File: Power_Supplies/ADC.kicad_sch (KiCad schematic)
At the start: 22 parts, among them IC3 PCM1865DBT, U17 LM27761

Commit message: big things are coming...
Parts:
- removed C57, C61: 1uF, Capacitor_SMD:C_0805_2012Metric, symbol Device:C
- removed C58: 10uF, Capacitor_SMD:C_0805_2012Metric, symbol Device:C
- removed C59: 2.2uF, Capacitor_SMD:C_0805_2012Metric, symbol Device:C
- removed C60: 4.7uF, Capacitor_SMD:C_0805_2012Metric, symbol Device:C
- removed R74: 249k, Resistor_SMD:R_0603_1608Metric, symbol Device:R
- removed R75: 499k, Resistor_SMD:R_0603_1608Metric, symbol Device:R
- removed U17: LM27761, Package_SON:WSON-8-1EP_2x2mm_P0.5mm_EP0.9x1.6mm, symbol Regulator_SwitchedCapacitor:LM27761
- added C18: 10uF, Capacitor_SMD:C_0805_2012Metric, symbol Device:C
- added C23, C24: 1uF, Capacitor_SMD:C_0805_2012Metric, symbol Device:C
- added C25: 4.7uF, Capacitor_SMD:C_0805_2012Metric, symbol Device:C
- added C26: 2.2uF, Capacitor_SMD:C_0805_2012Metric, symbol Device:C
- added R15: 249k, Resistor_SMD:R_0603_1608Metric, symbol Device:R
- added R16: 499k, Resistor_SMD:R_0603_1608Metric, symbol Device:R
- added U8: LM27761, Package_SON:WSON-8-1EP_2x2mm_P0.5mm_EP0.9x1.6mm, symbol Regulator_SwitchedCapacitor:LM27761
- renumbered C32 to C11, C102 to C12, C107 to C13, C110 to C14, C111 to C15, C112 to C16, C113 to C17, C114 to C19, C115 to C20, C116 to C21, C117 to C22, C118 to C27, C119 to C28, IC3 to IC1
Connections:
- net -5V: now also C26.2, R15.1, U8.4 (VOUT)
- net 5V: now also C18.2, C23.2, U8.1 (VIN), U8.6 (EN)
- net DGND: now also C18.1, C23.1, C25.1, C26.1, R16.2, U8.2 (GND), U8.9 (PAD)
- new net: C24.1, U8.7 (C-)
- new net: C24.2, U8.8 (C+)
- new net: R15.2, R16.1, U8.5 (VFB)
- new net: C25.2, U8.3 (CPOUT)

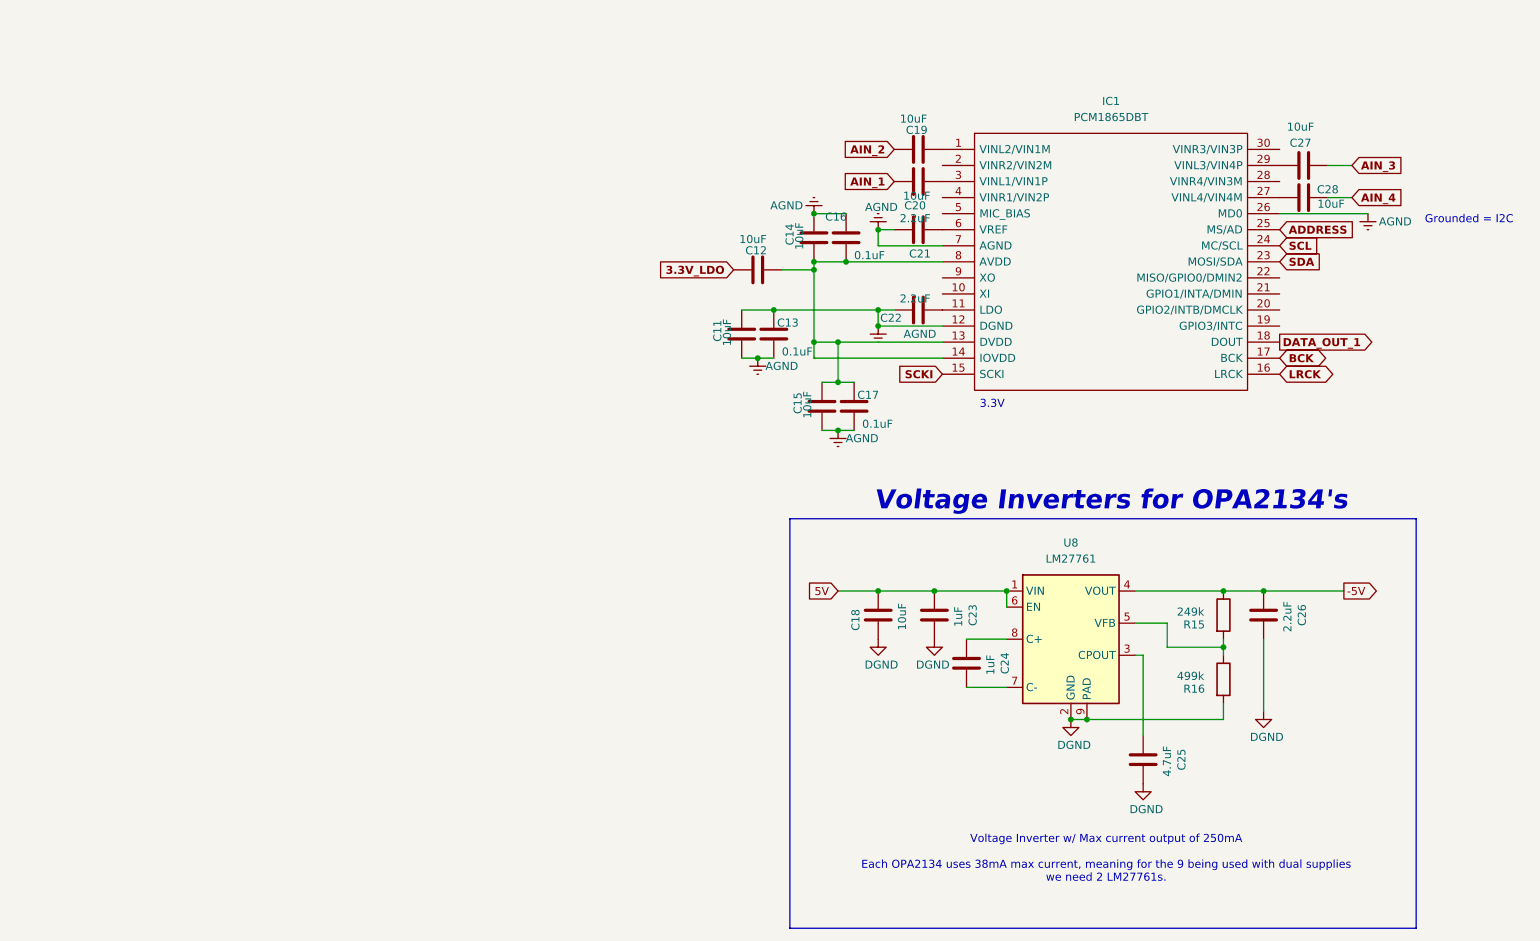
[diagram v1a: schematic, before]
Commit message: More XCORE PCB updates
Finished XTAG header, reinstated clock, worked on power pins
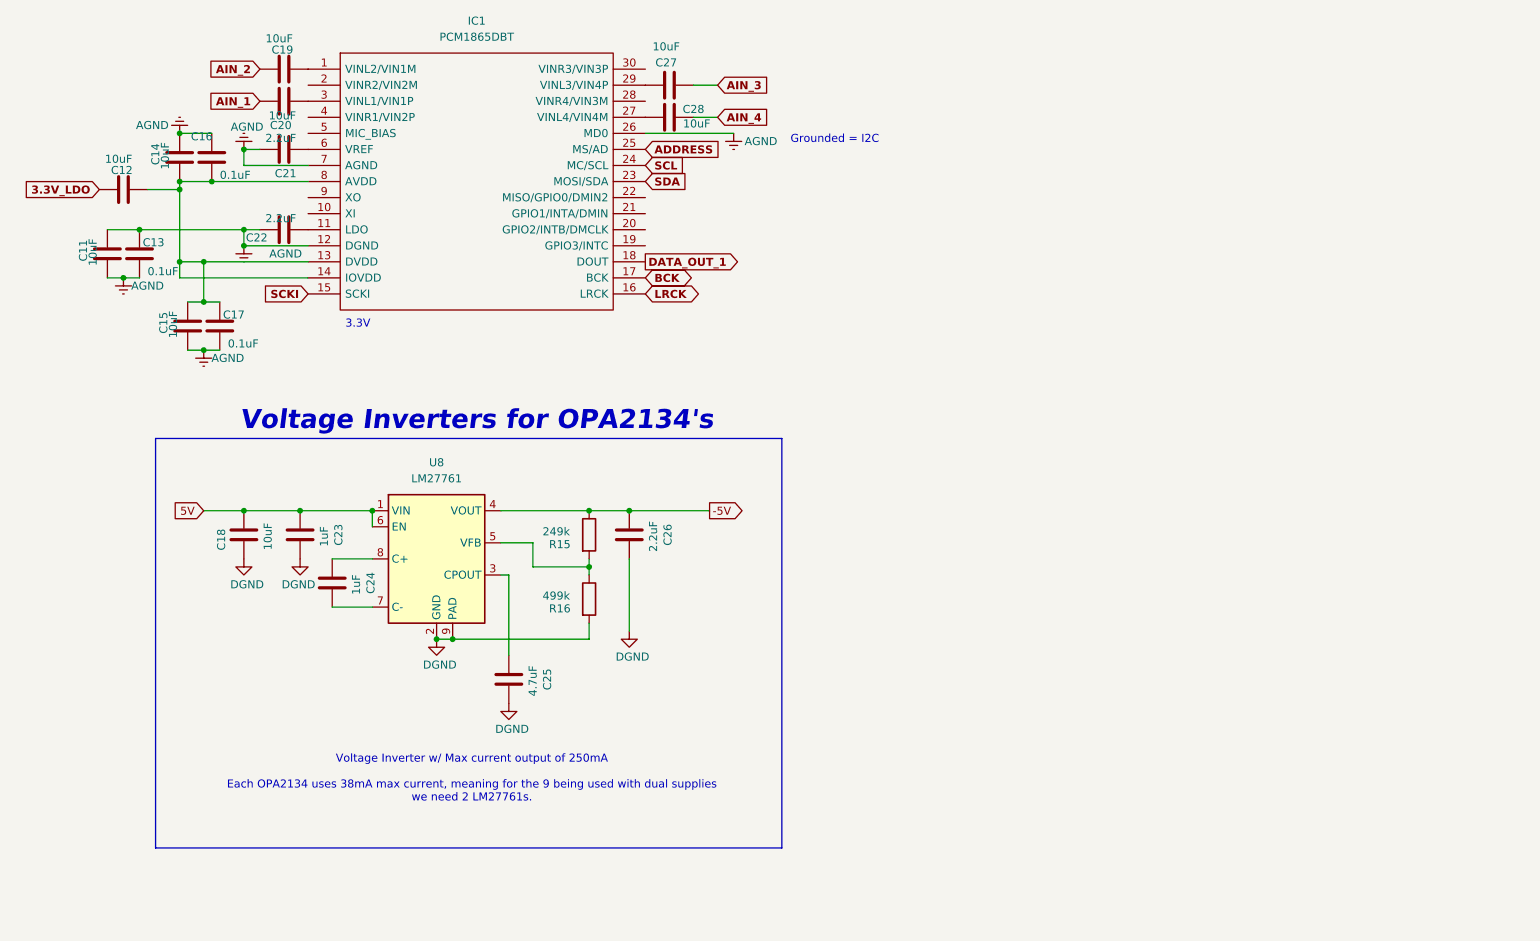
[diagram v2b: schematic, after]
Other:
- moved on the sheet: C11, C12, C13, C14, C15, C16, C17, C18, C19, C20, C21, C22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

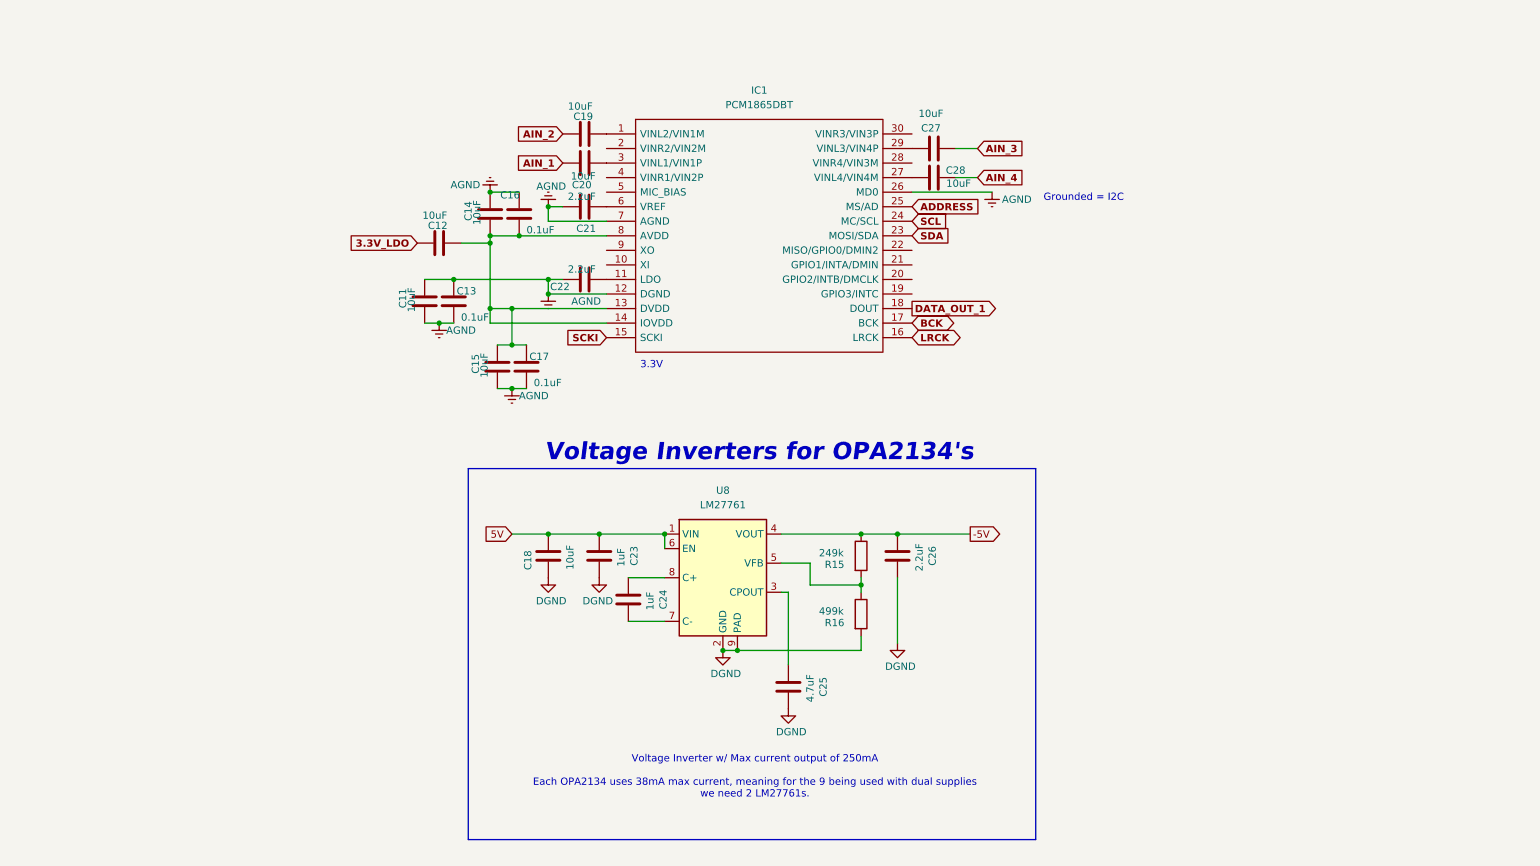
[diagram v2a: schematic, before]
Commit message: added both ADCs, added differential output to DACs
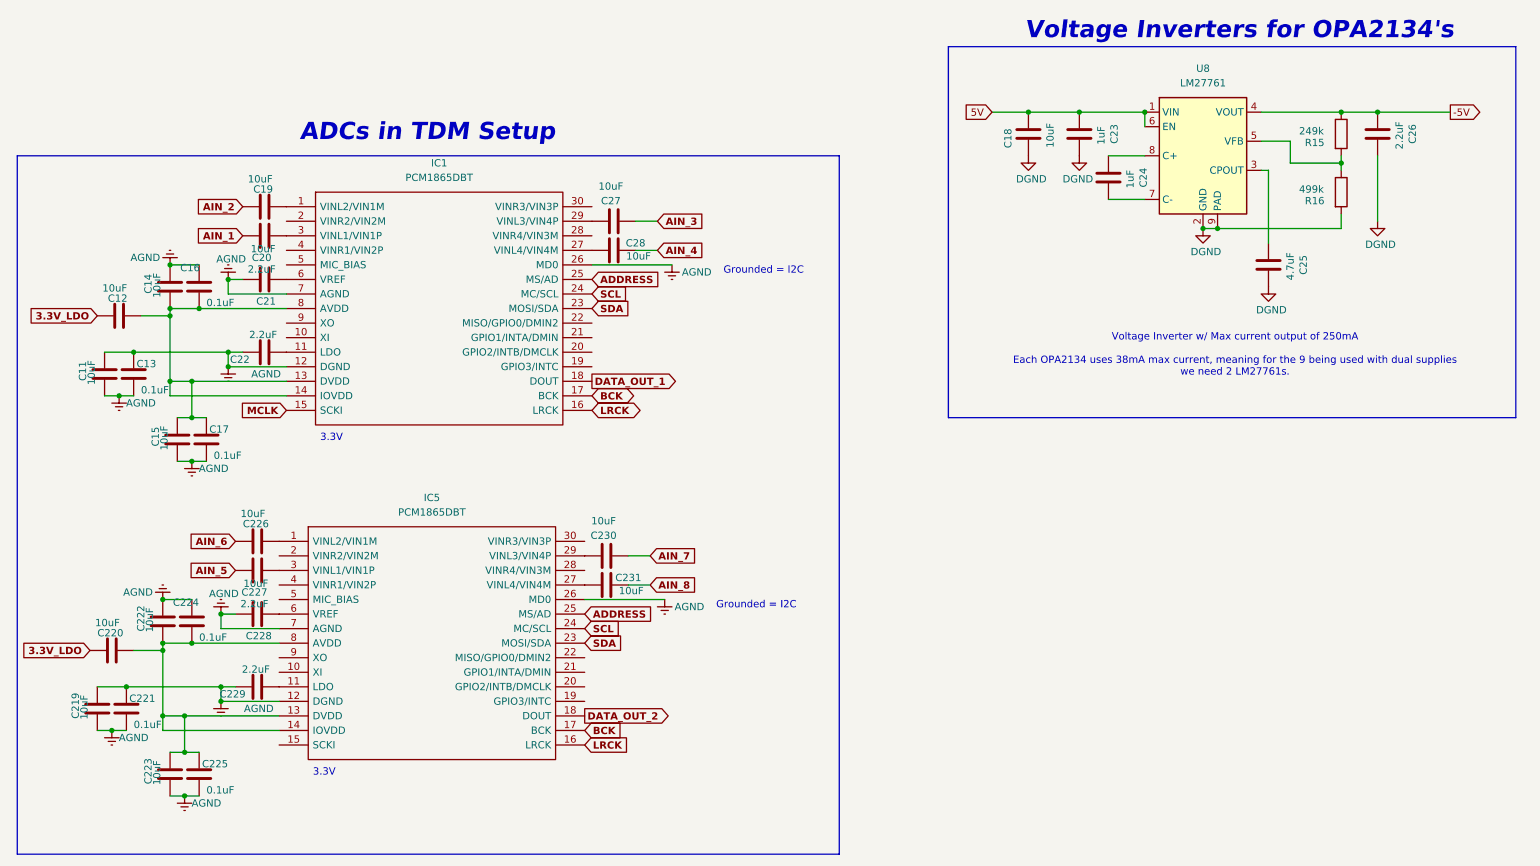
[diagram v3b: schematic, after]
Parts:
- added C219, C220, C222, C223, C226, C227, C230, C231: 10uF, Capacitor_SMD:C_0805_2012Metric, symbol Device:C
- added C221, C224, C225: 0.1uF, Capacitor_SMD:C_0805_2012Metric, symbol Device:C
- added C228, C229: 2.2uF, Capacitor_SMD:C_0805_2012Metric, symbol Device:C
- added IC5: PCM1865DBT, SamacSys_Parts:SOP50P640X120-30N, symbol SamacSys_Parts:PCM1865DBT
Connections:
- net 3.3V_LDO: now also C220.1
- net ADDRESS: now also IC5.25 (MS/AD)
- net AGND: now also C219.1, C219.2, C221.1, C221.2, C222.1, C223.2, C224.1, C225.2, C228.1, C229.1, IC5.12 (DGND), IC5.26 (MD0), IC5.7 (AGND)
- net BCK: now also IC5.17 (BCK)
- net LRCK: now also IC5.16 (LRCK)
- net SCL: now also IC5.24 (MC/SCL)
- net SDA: now also IC5.23 (MOSI/SDA)
- net SCKI renamed MCLK
- new net: C220.2, C222.2, C223.1, C224.2, C225.1, IC5.13 (DVDD), IC5.14 (IOVDD), IC5.8 (AVDD)
- new net: C229.2, IC5.11 (LDO)
- new net: C231.1, IC5.27 (VINL4/VIN4M)
- new net: C227.2, IC5.3 (VINL1/VIN1P)
- new net: C226.2, IC5.1 (VINL2/VIN1M)
- new net: C230.1, IC5.29 (VINL3/VIN4P)
- new net: C228.2, IC5.6 (VREF)
- new net AIN_5: C227.1
- new net AIN_6: C226.1
- new net AIN_7: C230.2
- new net AIN_8: C231.2
- new net DATA_OUT_2: IC5.18 (DOUT)
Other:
- note added: "ADCs in TDM Setup"
- moved on the sheet: C11, C12, C13, C14, C15, C16, C17, C18, C19, C20, C21, C22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

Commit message: Added stuff for the power supply circuitry
changed all grounds to GND (same ground plane)
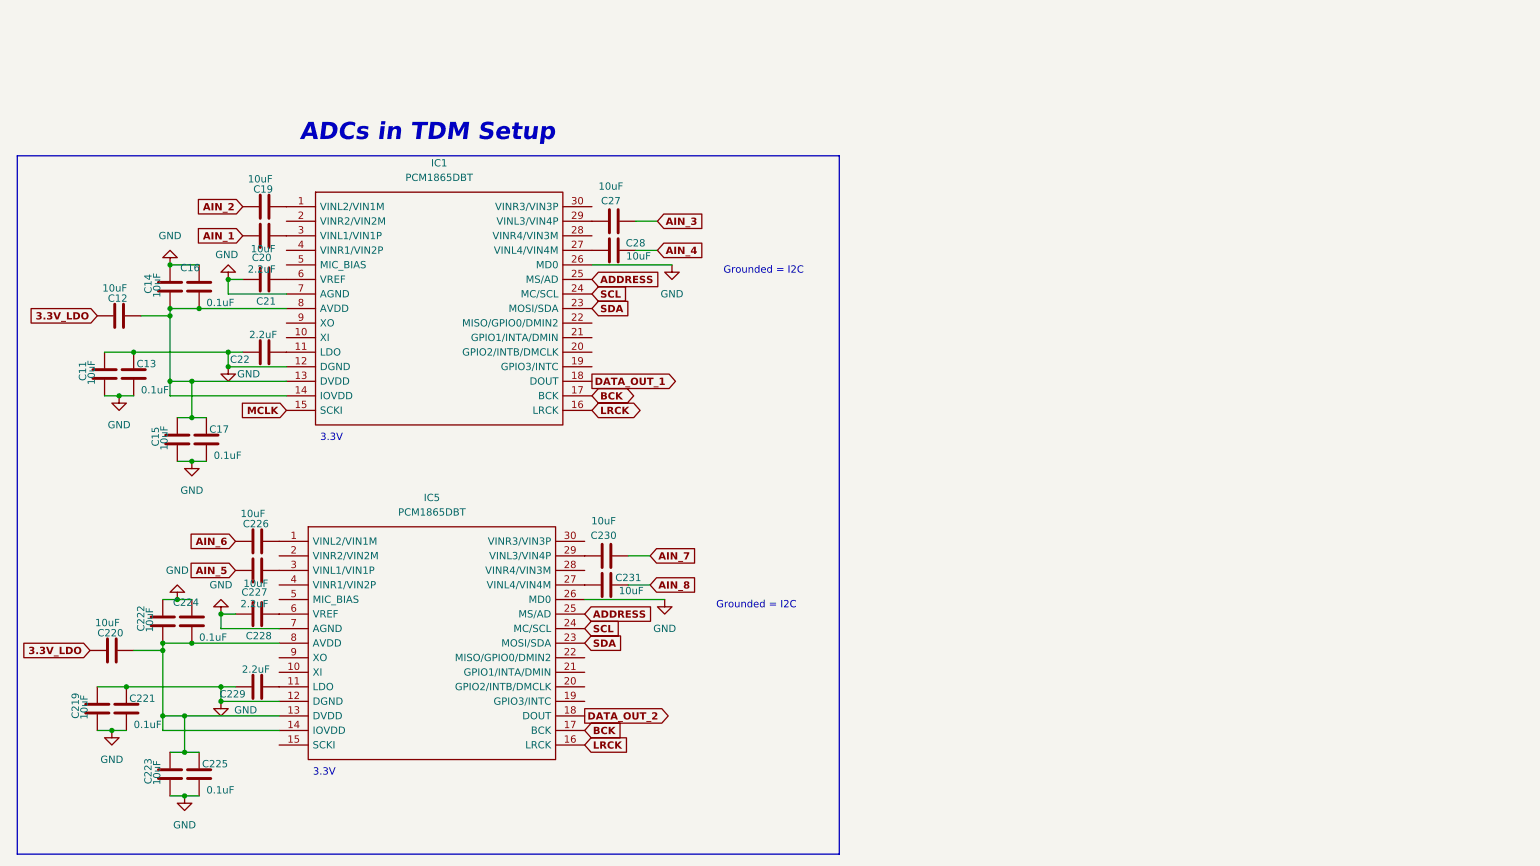
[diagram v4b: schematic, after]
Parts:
- removed C18: 10uF, Capacitor_SMD:C_0805_2012Metric, symbol Device:C
- removed C23, C24: 1uF, Capacitor_SMD:C_0805_2012Metric, symbol Device:C
- removed C25: 4.7uF, Capacitor_SMD:C_0805_2012Metric, symbol Device:C
- removed C26: 2.2uF, Capacitor_SMD:C_0805_2012Metric, symbol Device:C
- removed R15: 249k, Resistor_SMD:R_0603_1608Metric, symbol Device:R
- removed R16: 499k, Resistor_SMD:R_0603_1608Metric, symbol Device:R
- removed U8: LM27761, Package_SON:WSON-8-1EP_2x2mm_P0.5mm_EP0.9x1.6mm, symbol Regulator_SwitchedCapacitor:LM27761
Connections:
- net AGND renamed GND
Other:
- note removed: "Voltage Inverter w/ Max current output of 250mA Each OPA2134 uses 38mA max current, meaning for the 9 being used with dual supplies we need 2 LM27761s."
- note removed: "Voltage Inverters for OPA2134's"
